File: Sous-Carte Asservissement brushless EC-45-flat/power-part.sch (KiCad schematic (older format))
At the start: 7 parts, among them P5 5V, P6 8..24V, U1 MCP1702

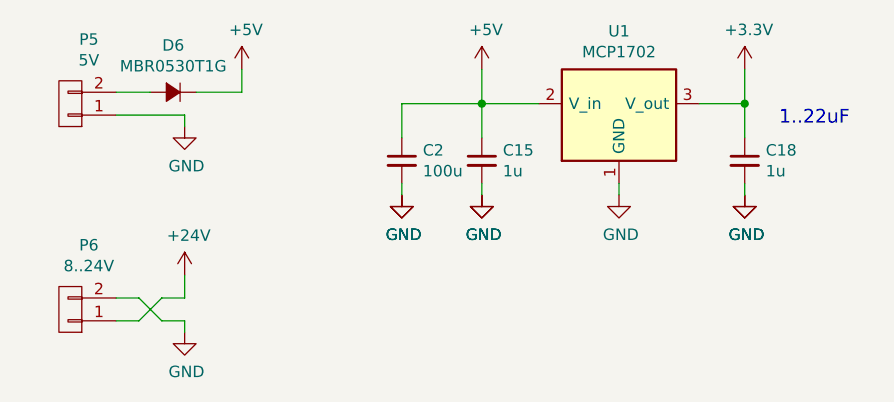
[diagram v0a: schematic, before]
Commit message: added B-plugs for power
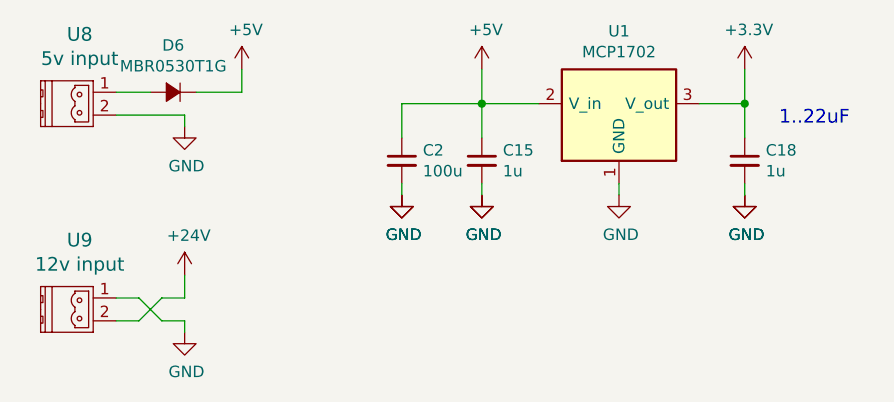
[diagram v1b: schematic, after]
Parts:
- removed P5: 5V, Connect:JWT_Vertical_A3963-RM3.96mm-2, symbol CONN_01X02
- removed P6: 8..24V, Connect:JWT_Vertical_A3963-RM3.96mm-2, symbol CONN_01X02
- added U8: 5v input, lib:B-plug-5mm, symbol B_Plug_5mm
- added U9: 12v input, lib:B-plug-5mm, symbol B_Plug_5mm
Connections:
- net +24V: now also U9.2
- net GND: now also U8.2, U9.1
- net at D6.2 (A): now also U8.1
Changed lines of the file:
@@
 $EndDescr
 $Comp
-L GND #PWR58
+L GND #PWR048
 U 1 1 5705D661
 P 4950 1800
-F 0 "#PWR58" H 4950 1550 50  0001 C CNN
+F 0 "#PWR048" H 4950 1550 50  0001 C CNN
 F 1 "GND" H 4958 1627 50  0000 C CNN
 F 2 "" H 4950 1800 50  0000 C CNN
@@
 	4350 1250 4350 1550
 $Comp
-L GND #PWR56
+L GND #PWR049
 U 1 1 5705D671
 P 4350 1800
-F 0 "#PWR56" H 4350 1550 50  0001 C CNN
+F 0 "#PWR049" H 4350 1550 50  0001 C CNN
 F 1 "GND" H 4358 1627 50  0000 C CNN
 F 2 "" H 4350 1800 50  0000 C CNN
@@
 $EndComp
 $Comp
-L GND #PWR57
+L GND #PWR050
 U 1 1 5705D694
 P 4350 1800
-F 0 "#PWR57" H 4350 1550 50  0001 C CNN
+F 0 "#PWR050" H 4350 1550 50  0001 C CNN
 F 1 "GND" H 4358 1627 50  0000 C CNN
 F 2 "" H 4350 1800 50  0000 C CNN
@@
 $EndComp
 $Comp
-L GND #PWR60
+L GND #PWR051
 U 1 1 5705D6A3
 P 5500 1800
-F 0 "#PWR60" H 5500 1550 50  0001 C CNN
+F 0 "#PWR051" H 5500 1550 50  0001 C CNN
 F 1 "GND" H 5508 1627 50  0000 C CNN
 F 2 "" H 5500 1800 50  0000 C CNN
@@
 $EndComp
 $Comp
-L GND #PWR61
+L GND #PWR052
 U 1 1 5705D6B2
 P 5500 1800
-F 0 "#PWR61" H 5500 1550 50  0001 C CNN
+F 0 "#PWR052" H 5500 1550 50  0001 C CNN
 F 1 "GND" H 5508 1627 50  0000 C CNN
 F 2 "" H 5500 1800 50  0000 C CNN
@@
 $EndComp
 $Comp
-L +5V #PWR55
+L +5V #PWR053
 U 1 1 5705D6E2
 P 4350 1250
-F 0 "#PWR55" H 4350 1100 50  0001 C CNN
+F 0 "#PWR053" H 4350 1100 50  0001 C CNN
 F 1 "+5V" H 4368 1423 50  0000 C CNN
 F 2 "" H 4350 1250 50  0000 C CNN
@@
 $EndComp
 $Comp
-L +3.3V #PWR59
+L +3.3V #PWR054
 U 1 1 5705D6F7
 P 5500 1250
-F 0 "#PWR59" H 5500 1100 50  0001 C CNN
+F 0 "#PWR054" H 5500 1100 50  0001 C CNN
 F 1 "+3.3V" H 5518 1423 50  0000 C CNN
 F 2 "" H 5500 1250 50  0000 C CNN
@@
 $EndComp
 $Comp
-L CONN_01X02 P6
-U 1 1 5705DCD6
-P 2550 2300
-F 0 "P6" H 2469 2019 50  0000 C CNN
-F 1 "8..24V" H 2469 2110 50  0000 C CNN
-F 2 "Connect:JWT_Vertical_A3963-RM3.96mm-2" H 2550 2300 50  0001 C CNN
-F 3 "" H 2550 2300 50  0000 C CNN
-	1    2550 2300
-	-1   0    0    1
-$EndComp
-$Comp
-L +24V #PWR50
+L +24V #PWR055
 U 1 1 5705DF9A
 P 3050 2150
-F 0 "#PWR50" H 3050 2000 50  0001 C CNN
+F 0 "#PWR055" H 3050 2000 50  0001 C CNN
 F 1 "+24V" H 3068 2323 50  0000 C CNN
 F 2 "" H 3050 2150 50  0000 C CNN
@@
 	3050 2250 3050 2150
 $Comp
-L GND #PWR51
+L GND #PWR056
 U 1 1 5705E164
 P 3050 2400
-F 0 "#PWR51" H 3050 2150 50  0001 C CNN
+F 0 "#PWR056" H 3050 2150 50  0001 C CNN
 F 1 "GND" H 3058 2227 50  0000 C CNN
 F 2 "" H 3050 2400 50  0000 C CNN
@@
 Wire Wire Line
 	3050 2400 3050 2350
-$Comp
-L CONN_01X02 P5
-U 1 1 57066A47
-P 2550 1400
-F 0 "P5" H 2469 1119 50  0000 C CNN
-F 1 "5V" H 2469 1210 50  0000 C CNN
-F 2 "Connect:JWT_Vertical_A3963-RM3.96mm-2" H 2550 1400 50  0001 C CNN
-F 3 "" H 2550 1400 50  0000 C CNN
-	1    2550 1400
-	-1   0    0    1
-$EndComp
 Wire Wire Line
 	3300 1350 3300 1250
 $Comp
-L GND #PWR49
+L GND #PWR057
 U 1 1 57066A55
 P 3050 1500
-F 0 "#PWR49" H 3050 1250 50  0001 C CNN
+F 0 "#PWR057" H 3050 1250 50  0001 C CNN
 F 1 "GND" H 3058 1327 50  0000 C CNN
 F 2 "" H 3050 1500 50  0000 C CNN
@@
 	3050 1450 2750 1450
 $Comp
-L +5V #PWR52
+L +5V #PWR058
 U 1 1 57066A78
 P 3300 1250
-F 0 "#PWR52" H 3300 1100 50  0001 C CNN
+F 0 "#PWR058" H 3300 1100 50  0001 C CNN
 F 1 "+5V" H 3318 1423 50  0000 C CNN
 F 2 "" H 3300 1250 50  0000 C CNN
@@
 1..22uF
 $Comp
-L GND #PWR53
+L GND #PWR059
 U 1 1 57070DDF
 P 4000 1800
-F 0 "#PWR53" H 4000 1550 50  0001 C CNN
+F 0 "#PWR059" H 4000 1550 50  0001 C CNN
 F 1 "GND" H 4008 1627 50  0000 C CNN
 F 2 "" H 4000 1800 50  0000 C CNN
@@
 $EndComp
 $Comp
-L GND #PWR54
+L GND #PWR060
 U 1 1 57070DEC
 P 4000 1800
-F 0 "#PWR54" H 4000 1550 50  0001 C CNN
+F 0 "#PWR060" H 4000 1550 50  0001 C CNN
 F 1 "GND" H 4008 1627 50  0000 C CNN
 F 2 "" H 4000 1800 50  0000 C CNN
@@
 Wire Wire Line
 	4000 1400 4600 1400
+$Comp
+L B_Plug_5mm U8
+U 1 1 57094931
+P 2650 1400
+F 0 "U8" H 2591 1703 60  0000 C CNN
+F 1 "5v input" H 2591 1597 60  0000 C CNN
+F 2 "lib:B-plug-5mm" H 2650 1400 60  0001 C CNN
+F 3 "" H 2650 1400 60  0000 C CNN
+	1    2650 1400
+	1    0    0    -1
+$EndComp
+$Comp
+L B_Plug_5mm U9
+U 1 1 57094D20
+P 2650 2300
+F 0 "U9" H 2591 2603 60  0000 C CNN
+F 1 "12v input" H 2591 2497 60  0000 C CNN
+F 2 "lib:B-plug-5mm" H 2650 2300 60  0001 C CNN
+F 3 "" H 2650 2300 60  0000 C CNN
+	1    2650 2300
+	1    0    0    -1
+$EndComp
 $EndSCHEMATC

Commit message: asser 1A : BOM + ready for pisa !
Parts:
- C2: footprint Capacitors_SMD:c_elec_6.3x4.5 -> Capacitors_SMD:c_elec_6.3x5.8
- D6: manf# (none) -> MBR0530T1G
- U1: manf# (none) -> MCP1702T-3302
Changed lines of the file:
@@
 F 2 "Diodes_SMD:SOD-123" V 3000 1350 50  0001 C CNN
 F 3 "" V 3000 1350 50  0000 C CNN
+F 4 "MBR0530T1G" H 3000 1350 60  0001 C CNN "manf#"
 	1    3000 1350
 	-1   0    0    1
@@
 F 0 "C2" H 4092 1696 50  0000 L CNN
 F 1 "100u" H 4092 1605 50  0000 L CNN
-F 2 "Capacitors_SMD:c_elec_6.3x4.5" H 4000 1650 50  0001 C CNN
+F 2 "Capacitors_SMD:c_elec_6.3x5.8" H 4000 1650 50  0001 C CNN
 F 3 "" H 4000 1650 50  0000 C CNN
 	1    4000 1650
@@
 F 2 "TO_SOT_Packages_SMD:SOT89-3_Housing" H 4950 1450 50  0001 C CNN
 F 3 "" H 4950 1450 50  0000 C CNN
+F 4 "MCP1702T-3302" H 4950 1450 60  0001 C CNN "manf#"
 	1    4950 1450
 	1    0    0    -1
